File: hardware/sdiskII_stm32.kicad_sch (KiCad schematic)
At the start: 34 parts, among them J2 APPLE_SDISKII, U1 74LS123, U2 MicroSD_SPI_CD, U3 74LS125, U4 74LS14, U5 74LS74, U6 74LS393, U7 74LS86, U8 DM-OLED096-636, U9 TLV76133DCY

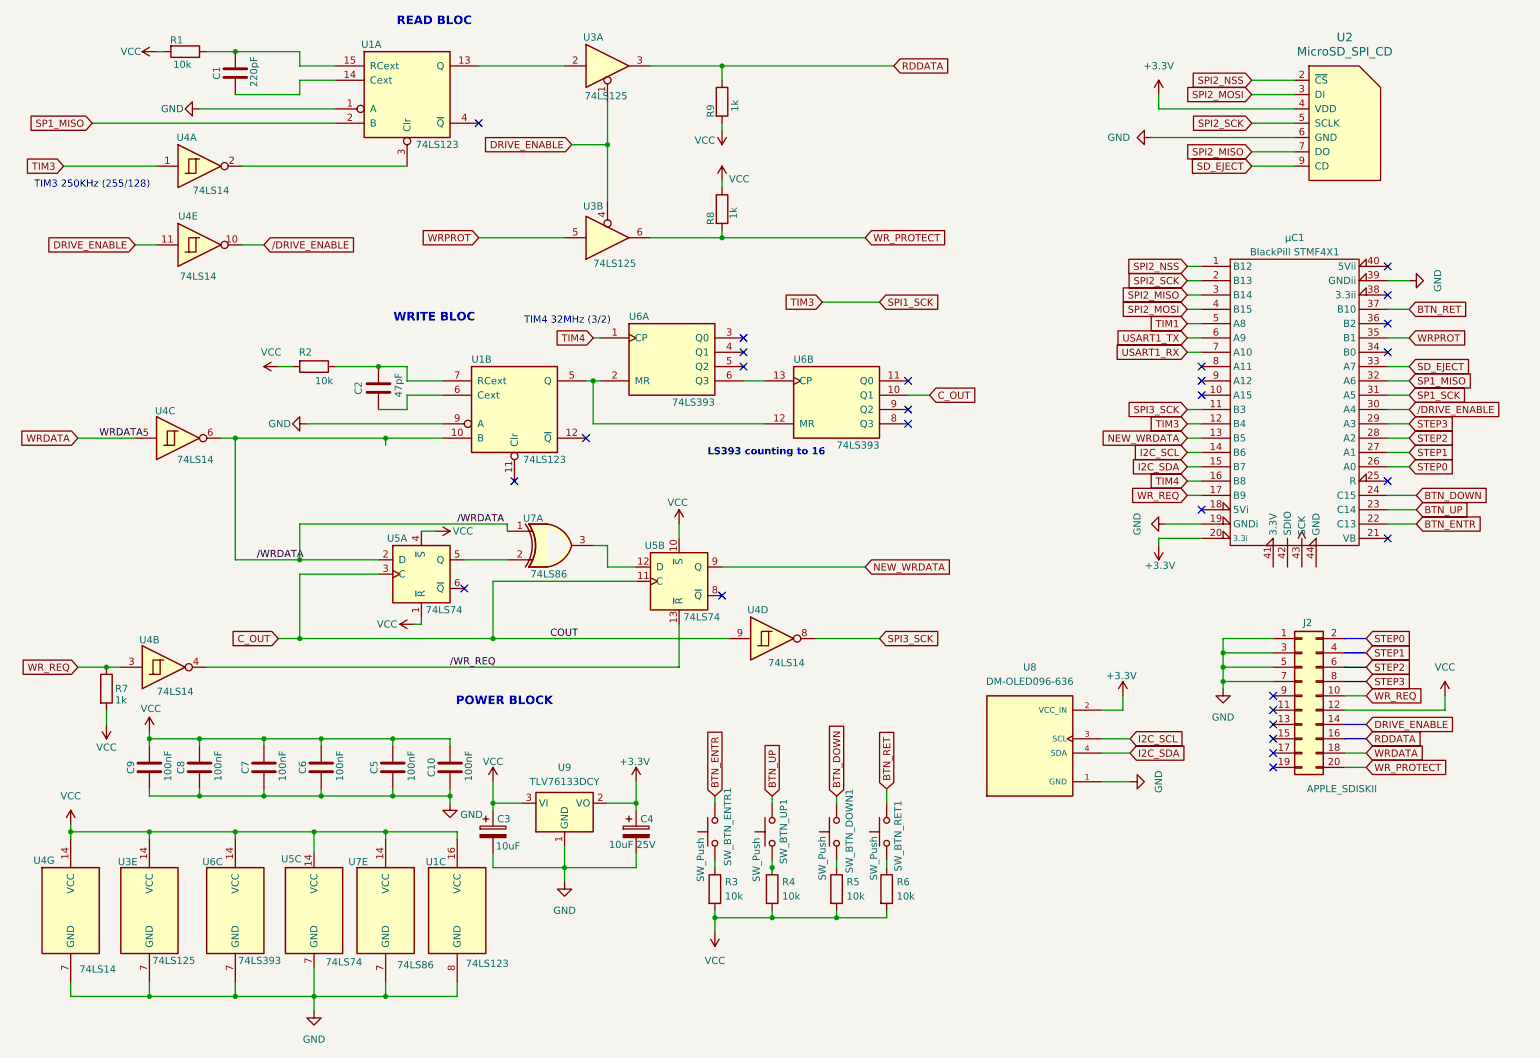
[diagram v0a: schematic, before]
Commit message: all images working
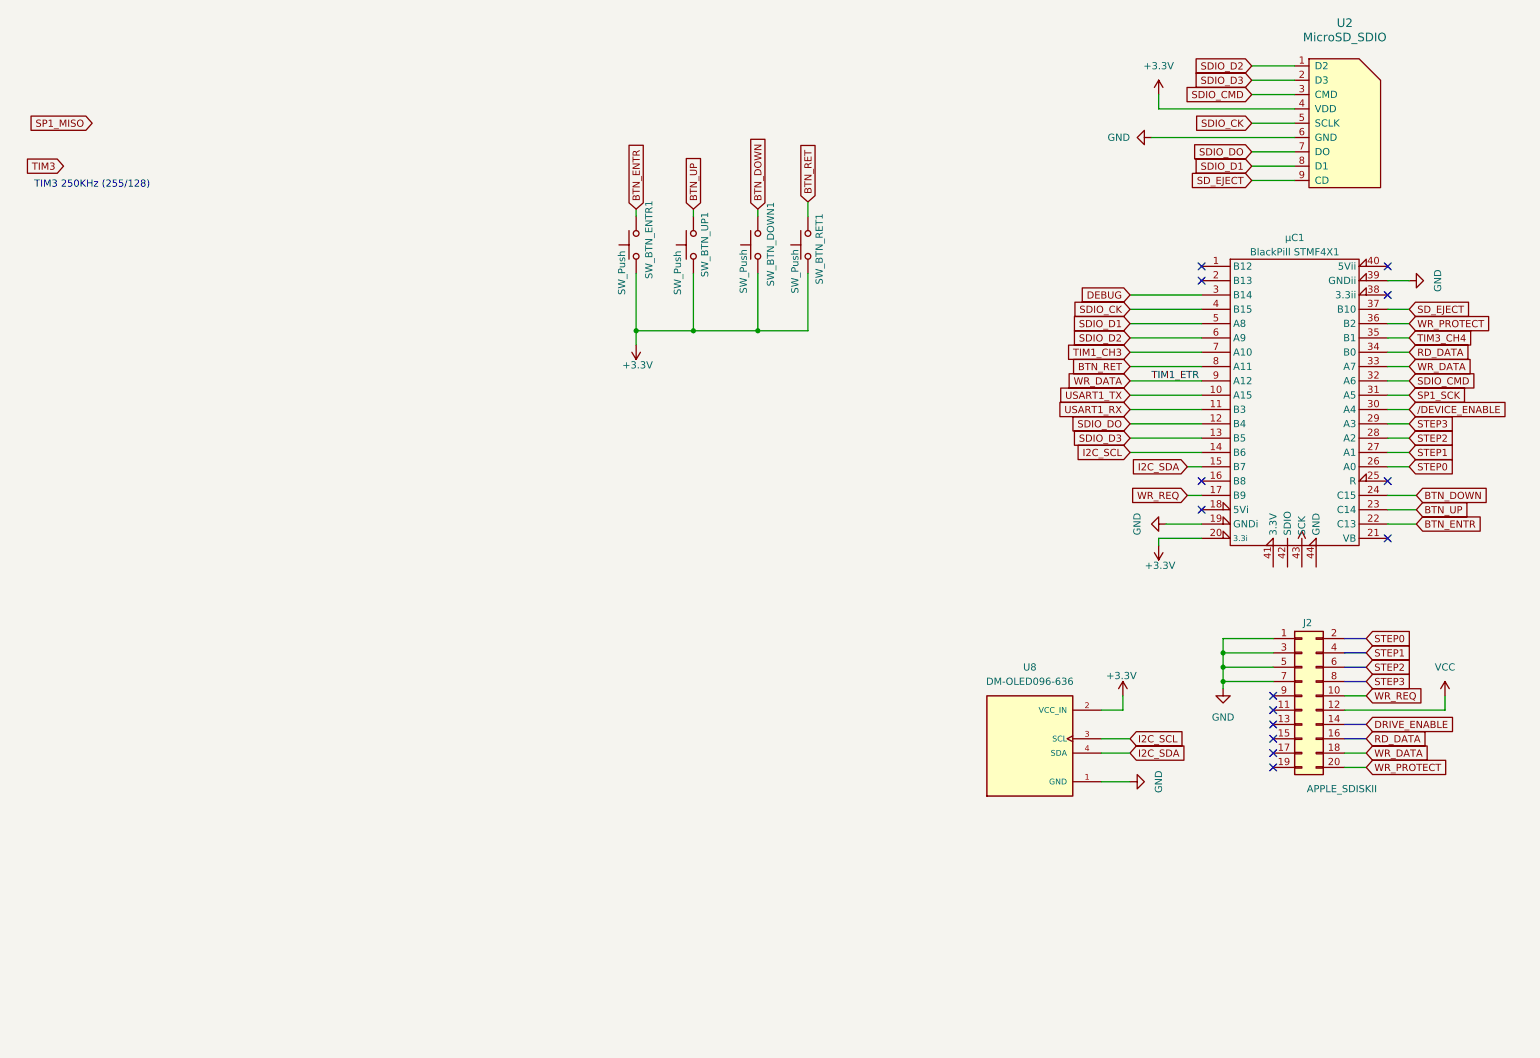
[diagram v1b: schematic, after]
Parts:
- removed C1: 220pF, Capacitor_THT:C_Disc_D5.0mm_W2.5mm_P5.00mm, symbol Device:C
- removed C10, C5, C6, C7, C8, C9: 100nF, Capacitor_THT:C_Disc_D5.0mm_W2.5mm_P5.00mm, symbol Device:C
- removed C2: 47pF, Capacitor_THT:C_Disc_D5.0mm_W2.5mm_P5.00mm, symbol Device:C
- removed C3: 10uF, Capacitor_THT:CP_Radial_D5.0mm_P2.50mm, symbol Device:C_Polarized
- removed C4: 10uF 25V, Capacitor_THT:CP_Radial_D5.0mm_P2.50mm, symbol Device:C_Polarized
- removed R1, R2, R3, R4, R5, R6: 10k, Resistor_THT:R_Axial_DIN0207_L6.3mm_D2.5mm_P7.62mm_Horizontal, symbol Device:R
- removed R7, R8, R9: 1k, Resistor_THT:R_Axial_DIN0207_L6.3mm_D2.5mm_P7.62mm_Horizontal, symbol Device:R
- removed U1: 74LS123, Package_DIP:DIP-16_W7.62mm, symbol 74xx:74LS123
- removed U3: 74LS125, Package_DIP:DIP-14_W7.62mm, symbol 74xx:74LS125
- removed U4: 74LS14, Package_DIP:DIP-14_W7.62mm, symbol 74xx:74LS14
- removed U5: 74LS74, Package_DIP:DIP-14_W7.62mm, symbol 74xx:74LS74
- removed U6: 74LS393, Package_DIP:DIP-14_W7.62mm, symbol 74xx:74LS393
- removed U7: 74LS86, Package_DIP:DIP-14_W7.62mm, symbol 74xx:74LS86
- removed U9: TLV76133DCY, Package_TO_SOT_SMD:SOT-223-3_TabPin2, symbol Regulator_Linear:TLV76133DCY
- U2: value MicroSD_SPI_CD -> MicroSD_SDIO
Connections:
- net SPI3_SCK is gone; now on net USART1_RX: μC1.11 (B3)
- net WRDATA is gone; now on net WR_DATA: J2.18 (Pin_18)
- net +3.3V: now also SW_BTN_DOWN1.1, SW_BTN_ENTR1.1, SW_BTN_RET1.1, SW_BTN_UP1.1
- net BTN_RET: now also μC1.8 (A11); no longer μC1.37 (B10)
- net SD_EJECT: now also μC1.37 (B10); no longer μC1.33 (A7)
- net SP1_MISO: no longer μC1.32 (A6)
- net USART1_RX: no longer μC1.7 (A10)
- net USART1_TX: now also μC1.10 (A15); no longer μC1.6 (A9)
- net WR_PROTECT: now also μC1.36 (B2)
- net RD_DATA: now reaches μC1.34 (B0)
- net WR_DATA: now reaches μC1.9 (A12)
- net WR_DATA: now also μC1.33 (A7)
- net NEW_WRDATA renamed SDIO_D3
- net SDIO_D3: now also U2.2 (D3)
- net SPI1_SCK renamed SDIO_DO
- net SDIO_DO: now also U2.7 (DO)
- net SPI2_MISO renamed DEBUG
- net DEBUG: no longer U2.7 (DO)
- net SPI2_MOSI renamed SDIO_CK
- net SDIO_CK: now also U2.5 (SCLK); no longer U2.3 (DI)
- net SPI2_NSS: no longer names the net of μC1.1 (B12)
- net SPI2_NSS: no longer U2.2 (~{CS})
- net SPI2_SCK: no longer names the net of μC1.2 (B13)
- net SPI2_SCK: no longer U2.5 (SCLK)
- net TIM1 renamed SDIO_D1
- net SDIO_D1: now also U2.8 (D1)
- net TIM4: no longer names the net of μC1.16 (B8)
- net WRPROT renamed TIM3_CH4
- net /DRIVE_ENABLE renamed /DEVICE_ENABLE
- new net SDIO_CMD: U2.3 (CMD), μC1.32 (A6)
- new net SDIO_D2: U2.1 (D2), μC1.6 (A9)
- new net TIM1_CH3: μC1.7 (A10)
- no-connect marks 27 -> 14
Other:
- note removed: "LS393 counting to 16"
- note removed: "POWER BLOCK"
- note removed: "READ BLOC"
- note removed: "TIM4 32MHz (3/2)"
- note removed: "WRITE BLOC"
- moved on the sheet: SW_BTN_DOWN1, SW_BTN_ENTR1, SW_BTN_RET1, SW_BTN_UP1

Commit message: new realease with gerber
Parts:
- added J1: PWR, Connector_PinHeader_2.54mm:PinHeader_1x02_P2.54mm_Vertical, symbol Connector:Conn_01x02_Pin
- added J3: DBG, Connector_PinHeader_2.54mm:PinHeader_1x05_P2.54mm_Vertical, symbol Connector:Conn_01x05_Pin
- added J4: UART, Connector_PinHeader_2.54mm:PinHeader_1x03_P2.54mm_Vertical, symbol Connector:Conn_01x03_Pin
- added J5: TIM, Connector_PinHeader_2.54mm:PinHeader_1x03_P2.54mm_Vertical, symbol Connector:Conn_01x03_Pin
- added J6: STLINK, Connector_PinHeader_2.54mm:PinHeader_1x04_P2.54mm_Vertical, symbol Connector:Conn_01x04_Pin
- added R1, R2, R3: 1k, Resistor_THT:R_Axial_DIN0207_L6.3mm_D2.5mm_P10.16mm_Horizontal, symbol Device:R
- U2: footprint sdisk_stm32:GCT-MEM2055-00-190-01-A -> sdisk_stm32:GCT-MEM2055-00-190-01-A_VIB
- μC1: footprint acheron_Hardware.pretty-master:Mini_F4X1_STM32 -> acheron_Hardware.pretty-master:Mini_F4X1_STM32_VIB
- renumbered SW_BTN_DOWN1 to DOWN1, SW_BTN_ENTR1 to ENTR1, SW_BTN_RET1 to RET1, SW_BTN_UP1 to UP1
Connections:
- net SP1_SCK is gone; now on net WR_DATA: μC1.31 (A5)
- net /DEVICE_ENABLE is gone; now on net DEVICE_ENABLE: μC1.30 (A4)
- net +3.3V: now also μC1.41 (3.3V), J6.1 (Pin_1)
- net BTN_DOWN: now also μC1.22 (C13); no longer μC1.24 (C15)
- net BTN_ENTR: now also μC1.24 (C15); no longer μC1.22 (C13)
- net BTN_RET: now also μC1.1 (B12); no longer μC1.8 (A11)
- net DEBUG: now also J5.3 (Pin_3)
- net GND: now also U2.10 (GND), U2.~, μC1.44 (GND), J4.3 (Pin_3), J6.4 (Pin_4)
- net RD_DATA: now also J2.16 (Pin_16), J3.5 (Pin_5)
- net SD_EJECT: now also μC1.2 (B13); no longer μC1.37 (B10)
- net STEP0: now also J2.2 (Pin_2)
- net STEP1: now also J2.4 (Pin_4)
- net STEP2: now also J2.6 (Pin_6)
- net STEP3: now also J2.8 (Pin_8)
- net TIM3_CH4: now also J5.2 (Pin_2)
- net USART1_RX: now also J4.2 (Pin_2)
- net USART1_TX: now also J4.1 (Pin_1)
- net VCC: now also J1.1 (Pin_1), R1.2, R2.1, R3.1
- net WR_DATA: now also J3.1 (Pin_1); no longer μC1.9 (A12)
- net WR_PROTECT: now also J3.2 (Pin_2), R1.1
- net WR_REQ: now also J3.4 (Pin_4), R2.2
- net DEVICE_ENABLE: now reaches J2.14 (Pin_14)
- net DEVICE_ENABLE: now also J3.3 (Pin_3), R3.2
- net PWR_IN: now reaches μC1.18 (5Vi)
- net PWR_IN: now also J1.2 (Pin_2)
- net SDIO: now reaches μC1.42 (SDIO)
- net SDIO: now also J6.2 (Pin_2)
- net SCK: now reaches μC1.43 (SCK)
- net SCK: now also J6.3 (Pin_3)
- net TIM1_CH3: no longer names the net of μC1.7 (A10)
- new net TIM2_CH3: J5.1 (Pin_1), μC1.37 (B10)
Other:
- note removed: "TIM3 250KHz (255/128)"
- moved on the sheet: DOWN1, ENTR1, J2, RET1, UP1

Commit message: board rev20
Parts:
- removed J3: DBG, Connector_PinHeader_2.54mm:PinHeader_1x05_P2.54mm_Vertical, symbol Connector:Conn_01x05_Pin
- removed J5: TIM, Connector_PinHeader_2.54mm:PinHeader_1x03_P2.54mm_Vertical, symbol Connector:Conn_01x03_Pin
- added BZ1: Buzzer, symbol Device:Buzzer
- added J3: Conn_01x06, Connector_PinHeader_2.54mm:PinHeader_1x06_P2.54mm_Vertical, symbol Connector_Generic:Conn_01x06
- added J5: Conn_01x04, Connector_PinHeader_2.54mm:PinHeader_1x04_P2.54mm_Vertical, symbol Connector_Generic:Conn_01x04
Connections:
- net DEBUG: now also μC1.7 (A10), J5.3 (Pin_3); no longer μC1.3 (B14)
- net DEVICE_ENABLE: now also J3.3 (Pin_3)
- net GND: now also BZ1.2 (-), J3.6 (Pin_6), J5.4 (Pin_4)
- net RD_DATA: now also J3.5 (Pin_5)
- net TIM2_CH3: now also J5.1 (Pin_1)
- net TIM3_CH4: now also J5.2 (Pin_2)
- net WR_DATA: now also J3.1 (Pin_1)
- net WR_PROTECT: now also J3.2 (Pin_2)
- net WR_REQ: now also J3.4 (Pin_4)
- new net TIM1_CH2N: BZ1.1 (+), μC1.3 (B14)
- no-connect marks 14 -> 13
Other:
- moved on the sheet: J4

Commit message: board rev2
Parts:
- BZ1: footprint (none) -> buzzer:AS-1201B-LF
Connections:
- net RD_DATA: now also J3.1 (Pin_1); no longer J3.5 (Pin_5)
- net WR_DATA: now also J3.5 (Pin_5); no longer J3.1 (Pin_1)
- net WR_PROTECT: now also J3.4 (Pin_4); no longer J3.2 (Pin_2)
- net WR_REQ: now also J3.2 (Pin_2); no longer J3.4 (Pin_4)
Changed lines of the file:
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@@
 	(wire
 		(pts
-			(xy 124.46 80.01) (xy 129.54 80.01)
+			(xy 175.26 113.03) (xy 182.88 113.03)
 		)
 		(stroke
@@
 	(wire
 		(pts
-			(xy 137.16 48.26) (xy 146.05 48.26)
+			(xy 124.46 80.01) (xy 129.54 80.01)
 		)
 		(stroke
@@
 	(wire
 		(pts
-			(xy 219.71 95.25) (xy 222.25 95.25)
+			(xy 137.16 48.26) (xy 146.05 48.26)
 		)
 		(stroke
@@
 	(wire
 		(pts
-			(xy 255.27 102.87) (xy 259.08 102.87)
+			(xy 219.71 95.25) (xy 222.25 95.25)
 		)
 		(stroke
@@
 	(wire
 		(pts
-			(xy 105.41 102.87) (xy 109.22 102.87)
+			(xy 255.27 102.87) (xy 259.08 102.87)
 		)
 		(stroke
@@
 	(wire
 		(pts
-			(xy 219.71 59.69) (xy 222.25 59.69)
+			(xy 105.41 102.87) (xy 109.22 102.87)
 		)
 		(stroke
@@
 	(wire
 		(pts
-			(xy 175.26 115.57) (xy 182.88 115.57)
+			(xy 219.71 59.69) (xy 222.25 59.69)
 		)
 		(stroke
@@
 	(wire
 		(pts
-			(xy 175.26 120.65) (xy 182.88 120.65)
-		)
-		(stroke
-			(width 0)
-			(type default)
-		)
-	)
-	(wire
-		(pts
 			(xy 182.88 95.25) (xy 182.88 96.52)
 		)
@@
 	(wire
 		(pts
+			(xy 175.26 115.57) (xy 182.88 115.57)
+		)
+		(stroke
+			(width 0)
+			(type default)
+		)
+	)
+	(wire
+		(pts
 			(xy 175.26 125.73) (xy 180.34 125.73)
 		)
@@
 	(wire
 		(pts
+			(xy 175.26 123.19) (xy 182.88 123.19)
+		)
+		(stroke
+			(width 0)
+			(type default)
+		)
+	)
+	(wire
+		(pts
 			(xy 146.05 43.18) (xy 146.05 48.26)
 		)
@@
 	(wire
 		(pts
-			(xy 256.54 36.83) (xy 261.62 36.83)
+			(xy 175.26 120.65) (xy 182.88 120.65)
 		)
 		(stroke
@@
 	(wire
 		(pts
-			(xy 231.14 26.67) (xy 238.76 26.67)
+			(xy 256.54 36.83) (xy 261.62 36.83)
 		)
 		(stroke
@@
 	(wire
 		(pts
-			(xy 255.27 74.93) (xy 259.08 74.93)
+			(xy 231.14 26.67) (xy 238.76 26.67)
 		)
 		(stroke
@@
 	(wire
 		(pts
-			(xy 175.26 113.03) (xy 182.88 113.03)
+			(xy 255.27 74.93) (xy 259.08 74.93)
 		)
 		(stroke
@@
 	(wire
 		(pts
-			(xy 175.26 123.19) (xy 182.88 123.19)
-		)
-		(stroke
-			(width 0)
-			(type default)
-		)
-	)
-	(wire
-		(pts
 			(xy 105.41 115.57) (xy 139.7 115.57)
 		)
@@
 	(global_label "WR_DATA"
 		(shape input)
-		(at 182.88 113.03 0)
+		(at 182.88 123.19 0)
 		(fields_autoplaced yes)
 		(effects
@@
 		)
 		(property "Intersheetrefs" "${INTERSHEET_REFS}"
-			(at 193.969 113.03 0)
+			(at 193.969 123.19 0)
 			(effects
 				(font
@@
 	(global_label "WR_PROTECT"
 		(shape input)
-		(at 182.88 115.57 0)
+		(at 182.88 120.65 0)
 		(fields_autoplaced yes)
 		(effects
@@
 		)
 		(property "Intersheetrefs" "${INTERSHEET_REFS}"
-			(at 197.7789 115.57 0)
+			(at 197.7789 120.65 0)
 			(effects
 				(font
@@
 	(global_label "WR_REQ"
 		(shape input)
-		(at 182.88 120.65 0)
+		(at 182.88 115.57 0)
 		(fields_autoplaced yes)
 		(effects
@@
 		)
 		(property "Intersheetrefs" "${INTERSHEET_REFS}"
-			(at 193.3037 120.65 0)
+			(at 193.3037 115.57 0)
 			(effects
 				(font
@@
 	(global_label "RD_DATA"
 		(shape input)
-		(at 182.88 123.19 0)
+		(at 182.88 113.03 0)
 		(fields_autoplaced yes)
 		(effects
@@
 		)
 		(property "Intersheetrefs" "${INTERSHEET_REFS}"
-			(at 193.7876 123.19 0)
+			(at 193.7876 113.03 0)
 			(effects
 				(font
@@
 			)
 		)
-		(property "Footprint" ""
+		(property "Footprint" "buzzer:AS-1201B-LF"
 			(at 155.575 146.05 90)
 			(effects

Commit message: v0.79 Smartport HD working
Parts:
- added JP1: SPST, Jumper:SolderJumper-2_P1.3mm_Open_RoundedPad1.0x1.5mm, symbol Jumper:SolderJumper_2_Open
- R1, R2, R3: now not fitted
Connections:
- net GND: no longer J2.7 (Pin_7)
- net PWR_IN: now also JP1.1 (A)
- net VCC: now also J2.11 (Pin_11), JP1.2 (B); no longer J2.12 (Pin_12)
- net SELECT: now reaches μC1.16 (B8)
- net SELECT: now also J2.12 (Pin_12)
- net 3.5DSK: now reaches μC1.8 (A11)
- net 3.5DSK: now also J2.7 (Pin_7)
- no-connect marks 13 -> 10
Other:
- title: APPLE II DISK EM STM32F401 -> APPLE II DISK EM STM32F411

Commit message: pcb small change v5
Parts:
- added D1: 1N4148, Diode_THT:D_DO-35_SOD27_P7.62mm_Horizontal, symbol Diode:1N4148
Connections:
- net PWR_IN: now also D1.1 (K); no longer J1.2 (Pin_2), JP1.1 (A)
- new net PWR_RD: D1.2 (A), J1.2 (Pin_2), JP1.1 (A)
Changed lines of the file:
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@@
 (kicad_sch
-	(version 20231120)
+	(version 20250114)
 	(generator "eeschema")
-	(generator_version "8.0")
+	(generator_version "9.0")
 	(paper "A4")
 	(title_block
 		(title "APPLE II DISK EM STM32F411")
-		(rev "21")
+		(rev "22")
 	)
 	(junction
@@
 	(wire
 		(pts
+			(xy 177.8 33.655) (xy 179.705 33.655)
+		)
+		(stroke
+			(width 0)
+			(type default)
+		)
+	)
+	(wire
+		(pts
+			(xy 168.275 33.655) (xy 170.18 33.655)
+		)
+		(stroke
+			(width 0)
+			(type default)
+		)
+	)
+	(wire
+		(pts
 			(xy 83.82 102.87) (xy 83.82 105.41)
 		)
@@
 	(wire
 		(pts
-			(xy 175.26 123.19) (xy 182.88 123.19)
+			(xy 174.625 45.72) (xy 179.07 45.72)
 		)
 		(stroke
@@
 	(wire
 		(pts
-			(xy 146.05 43.18) (xy 146.05 48.26)
+			(xy 175.26 123.19) (xy 182.88 123.19)
 		)
 		(stroke
@@
 	(wire
 		(pts
-			(xy 123.19 123.19) (xy 129.54 123.19)
+			(xy 146.05 43.18) (xy 146.05 48.26)
 		)
 		(stroke
@@
 	(wire
 		(pts
-			(xy 105.41 100.33) (xy 109.22 100.33)
+			(xy 123.19 123.19) (xy 129.54 123.19)
 		)
 		(stroke
@@
 	(wire
 		(pts
-			(xy 214.63 31.75) (xy 238.76 31.75)
+			(xy 105.41 100.33) (xy 109.22 100.33)
 		)
 		(stroke
@@
 	(wire
 		(pts
-			(xy 179.07 95.25) (xy 182.88 95.25)
+			(xy 214.63 31.75) (xy 238.76 31.75)
 		)
 		(stroke
@@
 	(wire
 		(pts
-			(xy 176.53 45.72) (xy 179.07 45.72)
+			(xy 179.07 95.25) (xy 182.88 95.25)
 		)
 		(stroke
@@
 		)
 	)
+	(global_label "PWR_RD"
+		(shape input)
+		(at 179.705 33.655 0)
+		(fields_autoplaced yes)
+		(effects
+			(font
+				(size 1.27 1.27)
+			)
+			(justify left)
+		)
+		(property "Intersheetrefs" "${INTERSHEET_REFS}"
+			(at 190.1892 33.655 0)
+			(effects
+				(font
+					(size 1.27 1.27)
+				)
+				(justify left)
+				(hide yes)
+			)
+		)
+	)
 	(global_label "WR_DATA"
 		(shape input)
@@
 	(global_label "PWR_IN"
 		(shape input)
-		(at 176.53 45.72 180)
+		(at 168.275 33.655 180)
 		(fields_autoplaced yes)
 		(effects
@@
 		)
 		(property "Intersheetrefs" "${INTERSHEET_REFS}"
-			(at 166.6505 45.72 0)
+			(at 158.3955 33.655 0)
 			(effects
 				(font
@@
 		)
 	)
+	(global_label "PWR_RD"
+		(shape input)
+		(at 174.625 45.72 180)
+		(fields_autoplaced yes)
+		(effects
+			(font
+				(size 1.27 1.27)
+			)
+			(justify right)
+		)
+		(property "Intersheetrefs" "${INTERSHEET_REFS}"
+			(at 164.1408 45.72 0)
+			(effects
+				(font
+					(size 1.27 1.27)
+				)
+				(justify right)
+				(hide yes)
+			)
+		)
+	)
 	(global_label "TIM2_CH3"
 		(shape input)
@@
 		)
 	)
-	(global_label "PWR_IN"
+	(global_label "PWR_RD"
 		(shape input)
 		(at 181.61 60.96 0)
@@
 		)
 		(property "Intersheetrefs" "${INTERSHEET_REFS}"
-			(at 191.4895 60.96 0)
+			(at 192.0942 60.96 0)
 			(effects
 				(font
@@
 	)
 	(symbol
+		(lib_id "Diode:1N4148")
+		(at 173.99 33.655 0)
+		(unit 1)
+		(exclude_from_sim no)
+		(in_bom yes)
+		(on_board yes)
+		(dnp no)
+		(fields_autoplaced yes)
+		(property "Reference" "D1"
+			(at 173.99 27.94 0)
+			(effects
+				(font
+					(size 1.27 1.27)
+				)
+			)
+		)
+		(property "Value" "1N4148"
+			(at 173.99 30.48 0)
+			(effects
+				(font
+					(size 1.27 1.27)
+				)
+			)
+		)
+		(property "Footprint" "Diode_THT:D_DO-35_SOD27_P7.62mm_Horizontal"
+			(at 173.99 33.655 0)
+			(effects
+				(font
+					(size 1.27 1.27)
+				)
+				(hide yes)
+			)
+		)
+		(property "Datasheet" "https://assets.nexperia.com/documents/data-sheet/1N4148_1N4448.pdf"
+			(at 173.99 33.655 0)
+			(effects
+				(font
+					(size 1.27 1.27)
+				)
+				(hide yes)
+			)
+		)
+		(property "Description" "100V 0.15A standard switching diode, DO-35"
+			(at 173.99 33.655 0)
+			(effects
+				(font
+					(size 1.27 1.27)
+				)
+				(hide yes)
+			)
+		)
+		(property "Sim.Device" "D"
+			(at 173.99 33.655 0)
+			(effects
+				(font
+					(size 1.27 1.27)
+				)
+				(hide yes)
+			)
+		)
+		(property "Sim.Pins" "1=K 2=A"
+			(at 173.99 33.655 0)
+			(effects
+				(font
+					(size 1.27 1.27)
+				)
+				(hide yes)
+			)
+		)
+		(pin "1"
+		)
+		(pin "2"
+		)
+		(instances
+			(project ""
+				(path "/a83c7550-2269-4fd8-90ce-2da165082457"
+					(reference "D1")
+					(unit 1)
+				)
+			)
+		)
+	)
+	(symbol
 		(lib_id "power:+3.3V")
 		(at 132.08 72.39 0)
@@
 		)
 	)
+	(embedded_fonts no)
 )

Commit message: v0.80.12 beta
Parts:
- added D2: 1N4148WT, Diode_SMD:D_0805_2012Metric_Pad1.15x1.40mm_HandSolder, symbol Diode:1N4148WT
- added R4, R5: 330, Resistor_SMD:R_0805_2012Metric_Pad1.20x1.40mm_HandSolder, symbol Device:R
- R1, R2, R3: now left out of the parts list
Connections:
- net 3.5DSK: now also R5.2; no longer J2.7 (Pin_7)
- net PWR_IN: now also D2.1 (K)
- net PWR_RD: now also D2.2 (A)
- net SELECT: now also R4.2; no longer J2.12 (Pin_12)
- new net 3.5DSK_D: J2.7 (Pin_7), R5.1
- new net SELECT_D: J2.12 (Pin_12), R4.1
